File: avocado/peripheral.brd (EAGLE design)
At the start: 47 x 20 mm, 9 parts

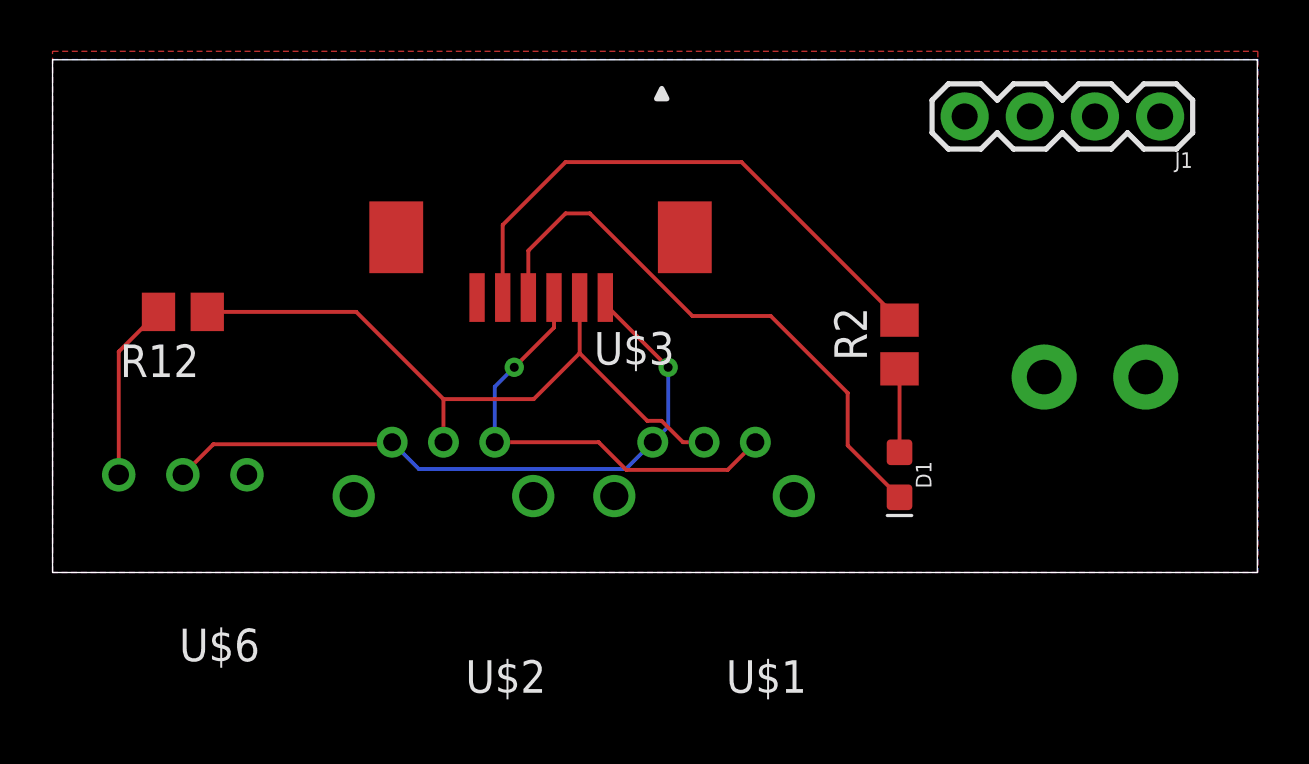
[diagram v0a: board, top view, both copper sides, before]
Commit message: fixed all airwires, still need to fix DRC
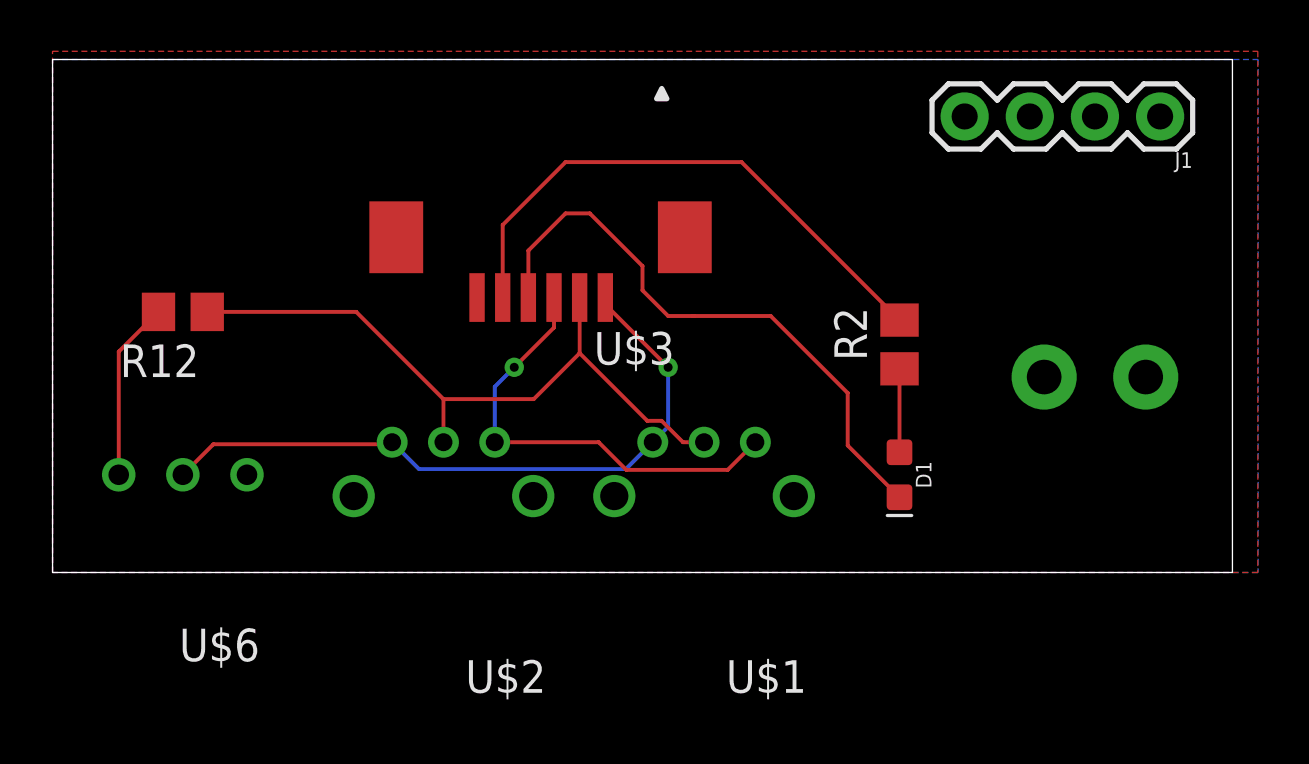
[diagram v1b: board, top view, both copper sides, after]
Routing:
- net GND: track 22.7 -> 23.2 mm
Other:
- board size 47 x 20 mm -> 46 x 20 mm
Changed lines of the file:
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@@
 <setting verticaltext="up"/>
 </settings>
-<grid distance="39.3700787" unitdist="mil" unit="mil" style="lines" multiple="1" display="no" altdistance="5" altunitdist="mil" altunit="mil"/>
+<grid distance="0.999999999" unitdist="mm" unit="mm" style="lines" multiple="1" display="no" altdistance="5" altunitdist="mil" altunit="mil"/>
 <layers>
 <layer number="1" name="Top" color="4" fill="1" visible="yes" active="yes"/>
@@
 <board>
 <plain>
-<wire x1="0" y1="0" x2="46.97" y2="0" width="0" layer="20"/>
-<wire x1="46.97" y1="0" x2="46.97" y2="19.99" width="0" layer="20"/>
-<wire x1="46.97" y1="19.99" x2="0" y2="19.99" width="0" layer="20"/>
-<wire x1="0" y1="19.99" x2="0" y2="0" width="0" layer="20"/>
+<wire x1="0" y1="0" x2="46" y2="0" width="0" layer="20"/>
+<wire x1="46" y1="0" x2="46" y2="20" width="0" layer="20"/>
+<wire x1="46" y1="20" x2="0" y2="20" width="0" layer="20"/>
+<wire x1="0" y1="20" x2="0" y2="0" width="0" layer="20"/>
 </plain>
 <attributes>
@@
 <wire x1="31" y1="4.953" x2="31" y2="7" width="0.1524" layer="1"/>
 <wire x1="31" y1="7" x2="28" y2="10" width="0.1524" layer="1"/>
-<wire x1="20.9467125" y1="14" x2="20" y2="14" width="0.1524" layer="1"/>
-<wire x1="24.9467125" y1="10" x2="20.9467125" y2="14" width="0.1524" layer="1"/>
-<wire x1="28" y1="10" x2="24.9467125" y2="10" width="0.1524" layer="1"/>
+<wire x1="20" y1="14" x2="20.9467125" y2="14" width="0.1524" layer="1"/>
+<wire x1="28" y1="10" x2="25" y2="10" width="0.1524" layer="1"/>
+<wire x1="25" y1="10" x2="24.9467125" y2="10" width="0.1524" layer="1"/>
 <wire x1="18.55" y1="12.55" x2="18.55" y2="10.72" width="0.1524" layer="1"/>
 <wire x1="20" y1="14" x2="18.55" y2="12.55" width="0.1524" layer="1"/>
+<wire x1="20.9467125" y1="14" x2="23" y2="11.9467125" width="0.1524" layer="1"/>
+<wire x1="23" y1="11.9467125" x2="23" y2="11" width="0.1524" layer="1"/>
+<wire x1="23" y1="11" x2="24" y2="10" width="0.1524" layer="1"/>
+<wire x1="24" y1="10" x2="24.9467125" y2="10" width="0.1524" layer="1"/>
 </signal>
 <signal name="GND_EXT">

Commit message: design that was ordered in first PCB run
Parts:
- U$3: value 0522070633 -> 5040500591; device avocado:1MM-FPC-6PIN -> avocado:5040500591
- moved J1 3.00 mm to (43.2, 14.8)
- moved U$3 0.97 mm to (19.0, 13.0), turned to 0 degrees
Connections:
- removed net GND_24V: J1.1, J1.2, U$5.GND
- removed net N$7: U$3.6
- net A: now also U$3.2; no longer U$3.1
- net B: now also U$3.1; no longer U$3.2
- net GND: now also J1.1, J1.2, U$5.GND
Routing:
- net GND: track 23.2 -> 4.42 mm, vias 0 -> 2
- net B: track 26.8 -> 30.8 mm
- net 3V3DC: track 21.9 -> 18.6 mm
- net A: track 26.6 -> 28.0 mm
- added copper zone on layer 16, net GND
- removed copper zone on layer 16, net GND_24V
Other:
- board size 46 x 20 mm -> 46 x 18 mm
- board text added: "ALLEN AKASH NATHAN RACHEL RYAN TSONG WEILIN"
- board text added: "AVOCADO V1.0 PERIPHERALS WILDCAT ROBOT DESIGN STUDIO"

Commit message: new gerber files and updated peripheral/main board
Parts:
- moved R2 6.46 mm to (26.6, 9.92)
- moved J1 6.35 mm to (36.8, 15.2)
- moved U$5 5.79 mm to (34.9, 8.05)
- moved D1 4.03 mm to (29.0, 3.35)
- moved U$1 2.79 mm to (22.9, 3.94)
- moved U$2 2.10 mm to (13.5, 3.94)
- moved U$6 0.83 mm to (4.48, 3.24)
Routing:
- net GND_EXT: track 17.2 -> 30.8 mm, vias 1 -> 2
- net 3V3DC: track 18.6 -> 11.8 mm
- net A: track 28.0 -> 25.1 mm, vias 1 -> 0
- net N$1: track 3.25 -> 5.72 mm
- net B: track 30.8 -> 31.7 mm
- net N$18: track 6.99 -> 7.81 mm
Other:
- board size 46 x 18 mm -> 39.5 x 18 mm

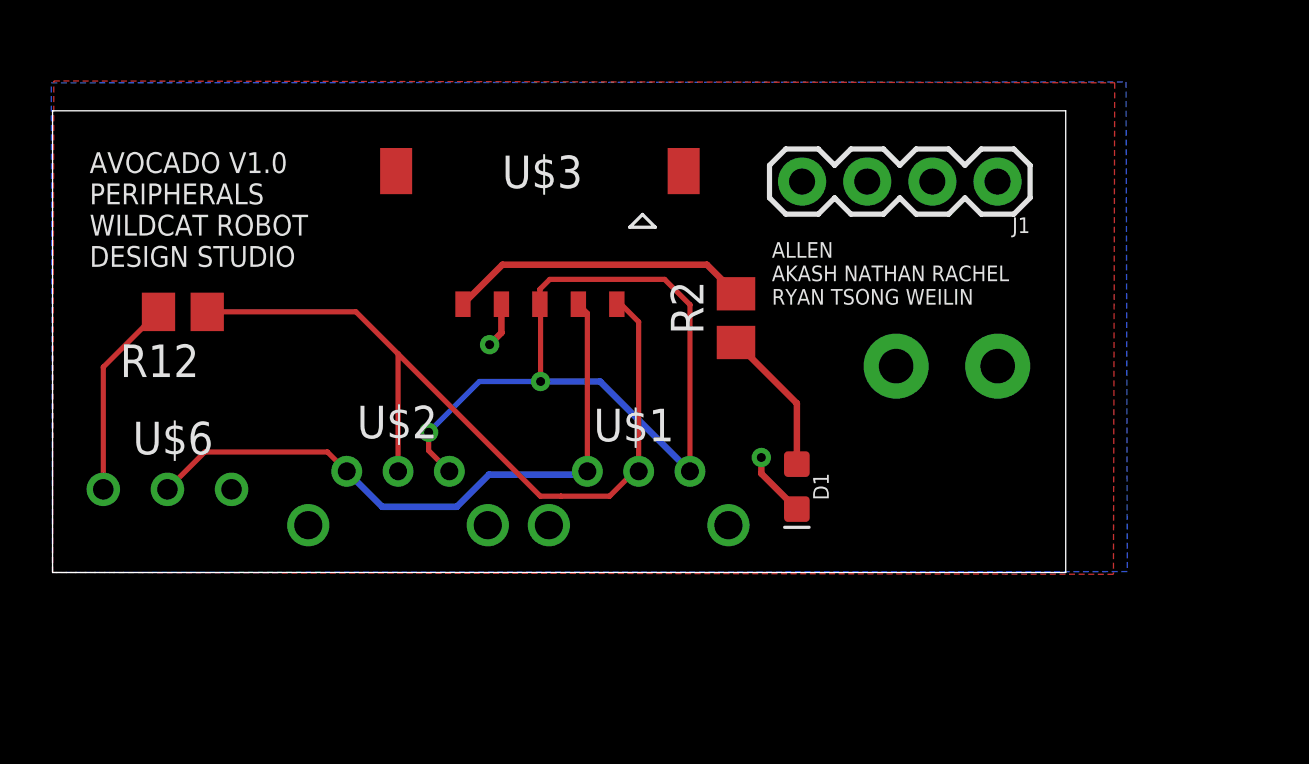
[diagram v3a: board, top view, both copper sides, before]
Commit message: modified peripheral board size
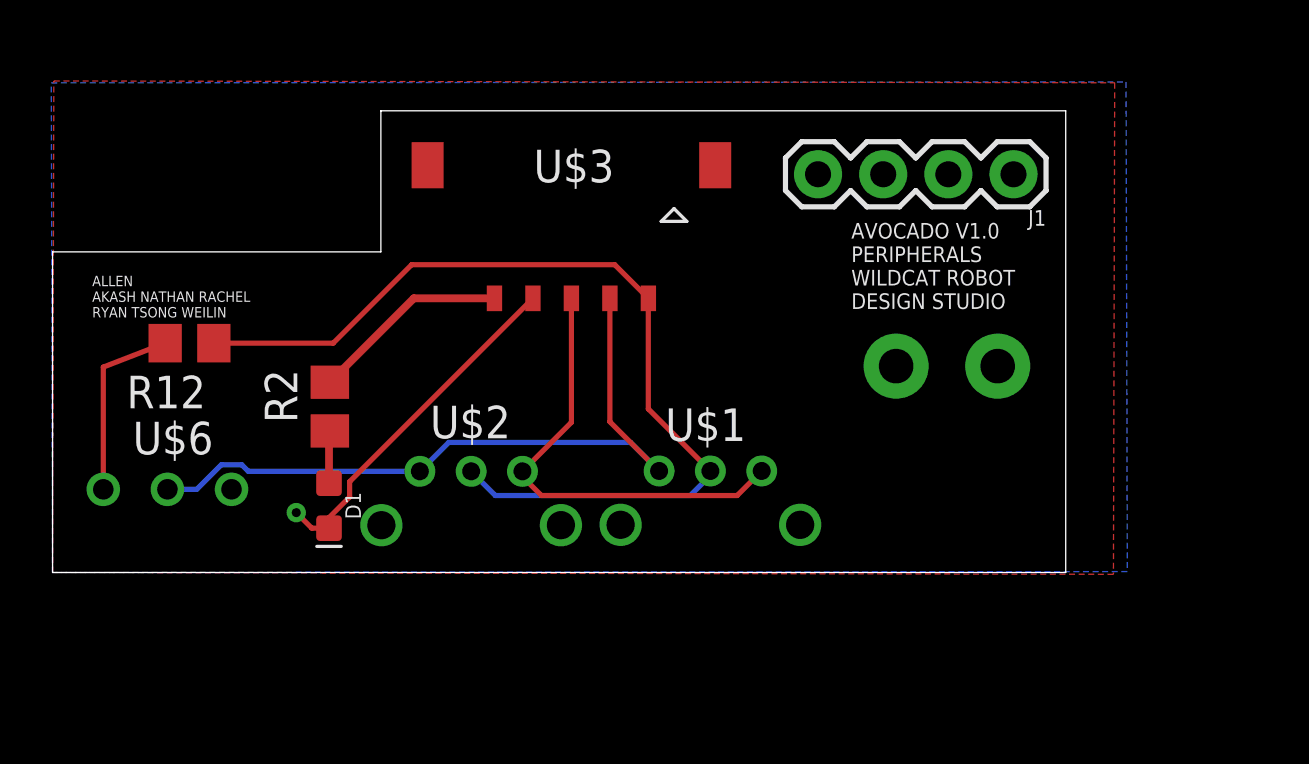
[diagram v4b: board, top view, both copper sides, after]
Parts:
- moved D1 18.3 mm to (10.8, 2.61)
- moved R2 16.2 mm to (10.8, 6.47)
- moved U$2 2.85 mm to (16.3, 3.94)
- moved U$1 2.80 mm to (25.6, 3.96)
- moved U$3 1.25 mm to (20.2, 13.2)
- moved R12 1.25 mm to (5.34, 8.94)
- moved J1 0.68 mm to (37.5, 15.5)
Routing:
- net GND_EXT: track 30.8 -> 17.8 mm, vias 2 -> 0
- net GND: track 4.35 -> 13.8 mm, vias 2 -> 1
- net B: track 31.7 -> 36.7 mm
- net 3V3DC: track 11.8 -> 7.77 mm
- net N$1: track 5.72 -> 2.05 mm
- net A: track 25.1 -> 28.1 mm
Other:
- outline, holes or cut-outs redrawn

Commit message: added mounting holes on peripheral board
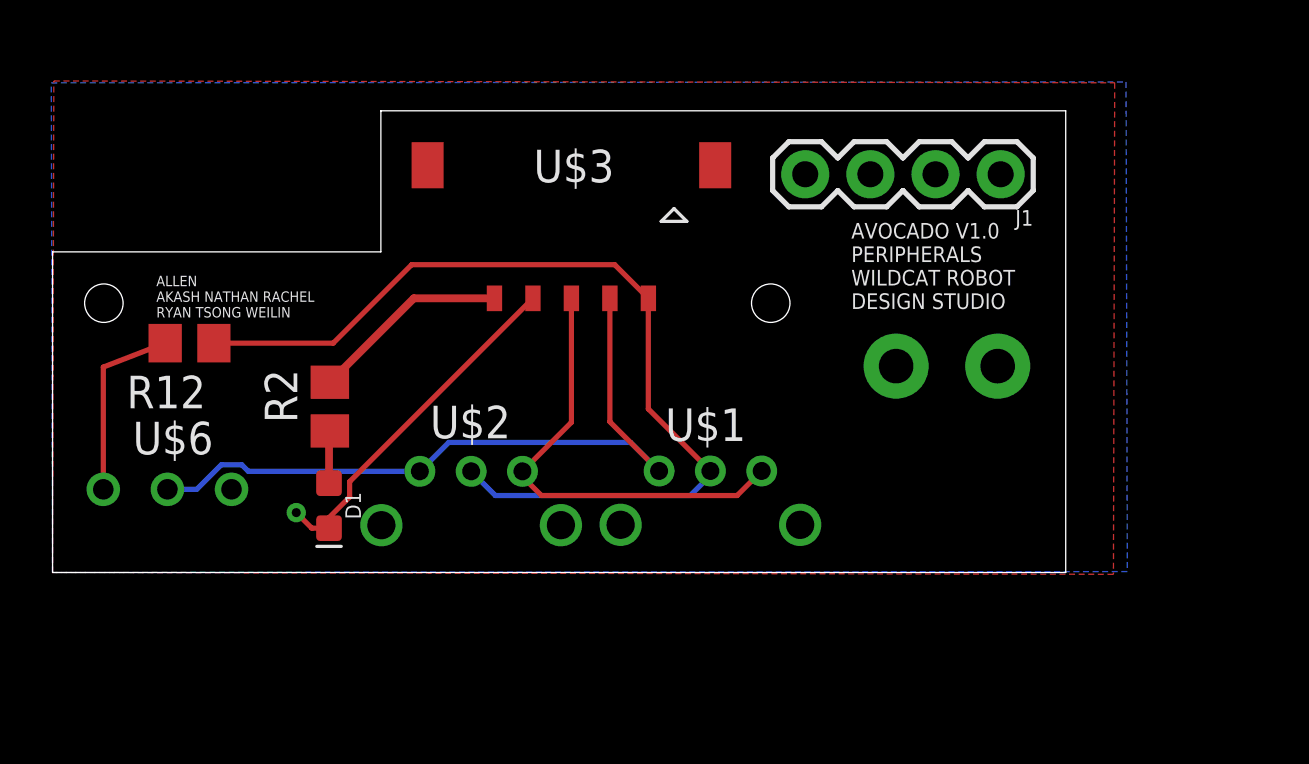
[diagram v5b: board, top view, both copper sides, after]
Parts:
- moved J1 0.50 mm to (37.0, 15.5)
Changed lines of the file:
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@@
 <setting verticaltext="up"/>
 </settings>
-<grid distance="19.6850394" unitdist="mil" unit="mil" style="lines" multiple="1" display="no" altdistance="5" altunitdist="mil" altunit="mil"/>
+<grid distance="0.500000001" unitdist="mm" unit="mm" style="lines" multiple="1" display="no" altdistance="5" altunitdist="mil" altunit="mil"/>
 <layers>
 <layer number="1" name="Top" color="4" fill="1" visible="yes" active="yes"/>
@@
 <layer number="43" name="vRestrict" color="2" fill="10" visible="no" active="yes"/>
 <layer number="44" name="Drills" color="7" fill="1" visible="no" active="yes"/>
-<layer number="45" name="Holes" color="7" fill="1" visible="no" active="yes"/>
+<layer number="45" name="Holes" color="7" fill="1" visible="yes" active="yes"/>
 <layer number="46" name="Milling" color="3" fill="1" visible="no" active="yes"/>
 <layer number="47" name="Measures" color="7" fill="1" visible="no" active="yes"/>
@@
 WILDCAT ROBOT
 DESIGN STUDIO</text>
-<text x="1.54413125" y="9.942740625" size="0.4064" layer="21">ALLEN
+<text x="4.04413125" y="9.942740625" size="0.4064" layer="21">ALLEN
 AKASH NATHAN RACHEL
 RYAN TSONG WEILIN</text>
@@
 <wire x1="12.8" y1="12.5" x2="12.8" y2="18" width="0" layer="20"/>
 <wire x1="12.8" y1="18" x2="39.5" y2="18" width="0" layer="20"/>
+<hole x="2" y="10.5" drill="1.5"/>
+<hole x="28" y="10.5" drill="1.5"/>
 </plain>
 <attributes>
@@
 <attribute name="PROD_ID" value="DIO-00821" x="10.778203125" y="2.6050875" size="1.778" layer="27" rot="R270" display="off"/>
 </element>
-<element name="J1" library="SparkFun-Connectors" package="1X04" value="" x="37.463865625" y="15.526484375" rot="R180">
-<attribute name="PROD_ID" value="CONN-09696" x="37.463865625" y="15.526484375" size="1.778" layer="27" rot="R180" display="off"/>
+<element name="J1" library="SparkFun-Connectors" package="1X04" value="" x="36.963865625" y="15.526484375" rot="R180">
+<attribute name="PROD_ID" value="CONN-09696" x="36.963865625" y="15.526484375" size="1.778" layer="27" rot="R180" display="off"/>
 </element>
 <element name="R12" library="rcl" library_urn="urn:adsk.eagle:library:334" package="R0805" package3d_urn="urn:adsk.eagle:package:23553/2" value="120" x="5.339209375" y="8.941159375" rot="R180">

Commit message: updated encoder and peripheral
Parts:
- moved U$1 2.30 mm to (25.6, 6.26)
- moved U$2 2.30 mm to (16.3, 6.24)
- moved R12 1.58 mm to (4.84, 7.44)
- moved U$5 0.97 mm to (34.9, 9.02)
- moved U$3 0.12 mm to (20.2, 13.3)
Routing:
- net GND: track 13.8 -> 3.34 mm, vias 1 -> 2
- net B: track 36.7 -> 39.8 mm
- net N$18: track 7.35 -> 5.55 mm
- net GND_EXT: track 17.8 -> 19.1 mm
- net A: track 28.1 -> 26.8 mm
